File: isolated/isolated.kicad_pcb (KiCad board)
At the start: 2 copper layers, 110 x 33.8 mm, 59 parts, among them J1 Screw_Terminal_01x02, J2 Screw_Terminal_01x02, Q1 IRF3205, Q2 IRF3205, U1 LTC3723, U2 TCMT1103, U3 LT1431, U4 MCP1792x-5002xCB

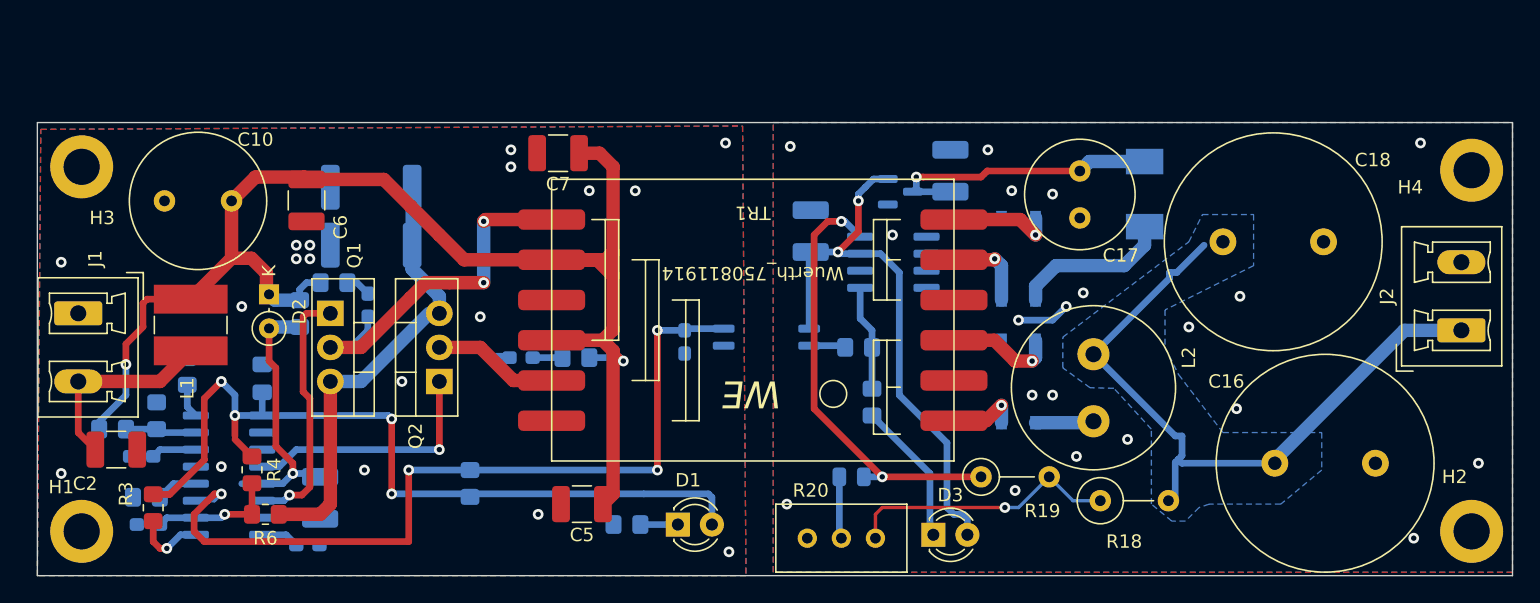
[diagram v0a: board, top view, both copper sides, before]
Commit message: kicad: Minor cleanups
- Replace LT1431 with TL431.

Signed-off-by: Patrick Rudolph <rudolphpatrick05@gmail.com>
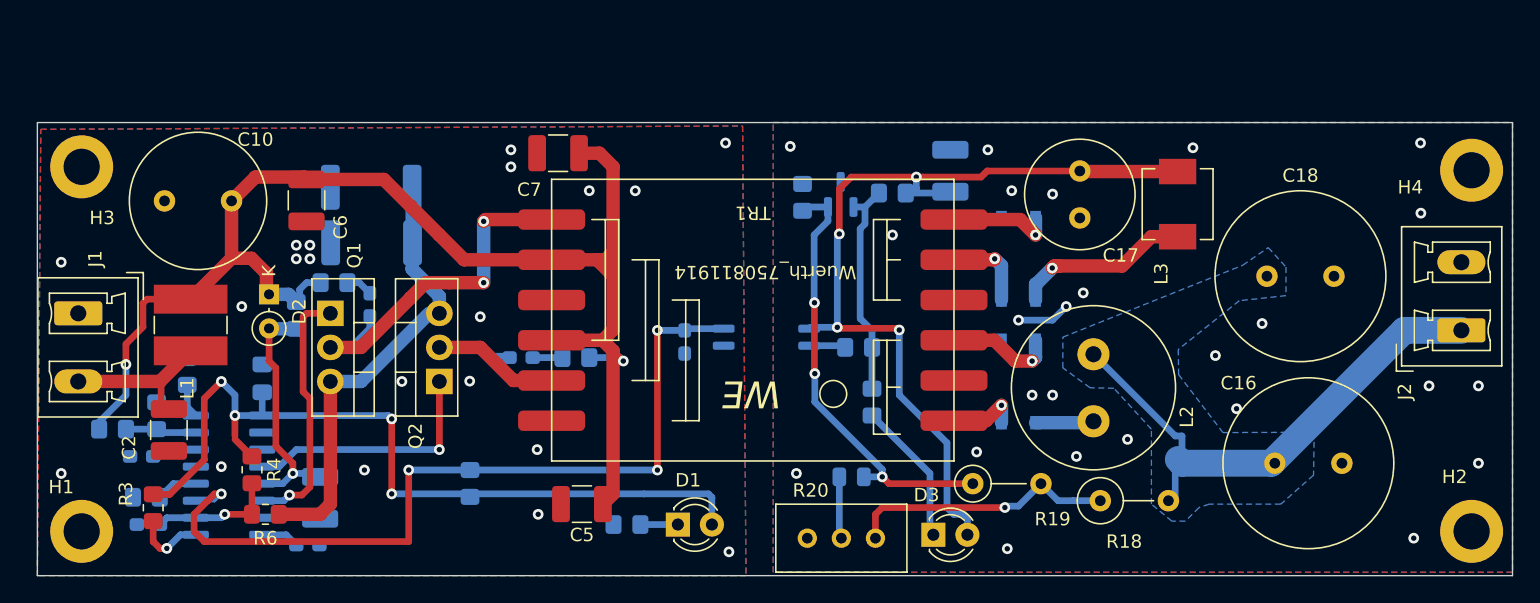
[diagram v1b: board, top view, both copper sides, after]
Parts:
- removed C19: 2u2, Capacitor_SMD:C_1210_3225Metric_Pad1.33x2.70mm_HandSolder
- removed U4: MCP1792x-5002xCB, Package_TO_SOT_SMD:SOT-23
- added R21: 10k, Resistor_SMD:R_0805_2012Metric_Pad1.20x1.40mm_HandSolder, B.Cu at (168.1, 40.3)
- added R22: 7k6, Resistor_SMD:R_0805_2012Metric_Pad1.20x1.40mm_HandSolder, B.Cu at (161.4, 40.6)
- C10: value C_Polarized -> 100u
- C16, C18: footprint Capacitor_THT:C_Radial_D16.0mm_H25.0mm_P7.50mm -> Capacitor_THT:C_Radial_D12.5mm_H20.0mm_P5.00mm
- C17: value 100u -> 10u
- L3: moved to F.Cu
- Q1, Q2: value IRF3205 -> IRLIZ 34N
- R15: value 330 -> 1k2
- R16: value 1k -> 3k3
- U3: value LT1431 -> TL431DBZ; footprint Package_SO:SOIC-8_3.9x4.9mm_P1.27mm -> Package_TO_SOT_SMD:SOT-23
- moved U3 6.40 mm to (164.3, 40.4), turned to 90 degrees
- moved C2 4.19 mm to (114.2, 58.0), turned to -90 degrees
- moved C18 4.16 mm to (196.1, 46.5)
- moved L3 2.57 mm to (189.4, 41.1)
- moved R19 0.80 mm to (174.1, 62.0)
- moved R2 0.29 mm to (123.7, 49.4)
- moved R11 0.18 mm to (129.3, 44.0)
- moved C11 0.15 mm to (129.2, 48.6)
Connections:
- C18 pad 2: Net-(C16-Pad1) -> GNDPWR
- D3 pad 2: +5VA -> VDD
- U2 pad 1: +5VA -> VDD
- U3 pad 2: unconnected-(U3-Pad2) -> /RTOP
- U3 pad 3: +5VA -> GNDPWR
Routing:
- net VDD: track 22.5 -> 66.0 mm, vias 1 -> 4
- net +5VA: track 42.7 -> 0.00 mm, vias 2 -> 0
- net Net-(C16-Pad1): track 51.1 -> 39.2 mm
- net Net-(R15-Pad2): track 7.89 -> 16.4 mm
- net Net-(C2-Pad1): track 14.9 -> 11.4 mm
- net /VIN: track 106.5 -> 103.2 mm
- net +10V: track 20.1 -> 18.3 mm
- net Net-(D5-Pad1): track 11.8 -> 13.2 mm, vias 0 -> 1
- net Net-(R10-Pad2): track 3.18 -> 2.55 mm
- net /RTOP: track 33.2 -> 33.0 mm, vias 2 -> 3
- net GNDPWR: vias 20 -> 25
- net GND: vias 18 -> 20

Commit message: kicad: Fix issues found in v0.1
- Change SOIC to SSOP package
- Fix MB4S pinout

Signed-off-by: Patrick Rudolph <rudolphpatrick05@gmail.com>
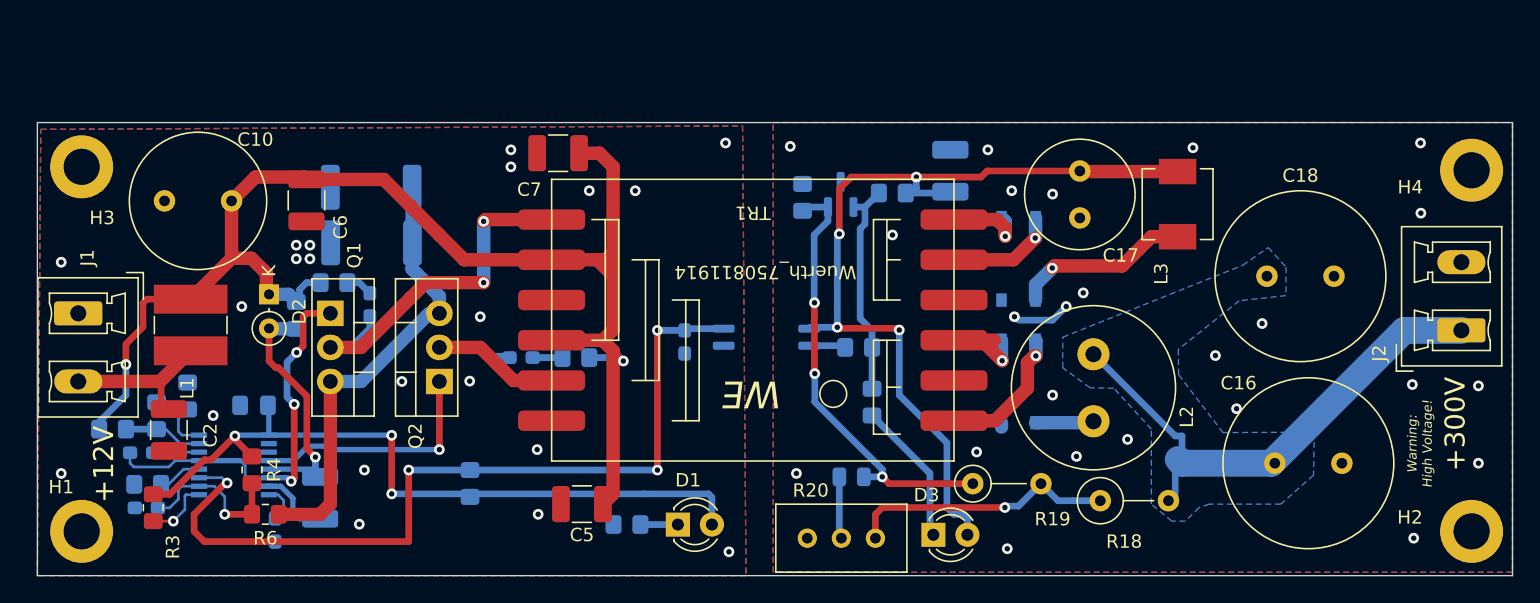
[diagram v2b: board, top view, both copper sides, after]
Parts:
- D5: value MB2S -> MB4S
- U1: footprint Package_SO:SOIC-16_3.9x9.9mm_P1.27mm -> Package_SO:SSOP-16_3.9x4.9mm_P0.635mm
- moved C4 2.68 mm to (122.1, 65.4), turned to -90 degrees
- moved C3 2.10 mm to (120.5, 56.1), turned to 0 degrees
- moved R10 1.83 mm to (115.6, 55.4)
- moved C8 1.25 mm to (112.5, 63.8)
- moved R7 0.97 mm to (112.6, 62.0)
- moved U1 0.85 mm to (119.0, 60.6)
- moved C12 0.28 mm to (112.2, 59.7)
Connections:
- D4 pad 2: Net-(D4-Pad2) -> GNDPWR
- D4 pad 3: GNDPWR -> Net-(TR1-Pad3)
- D4 pad 4: Net-(D4-Pad4) -> Net-(TR1-Pad1)
- D5 pad 2: Net-(D5-Pad2) -> GNDPWR
- D5 pad 3: GNDPWR -> Net-(TR1-Pad6)
- D5 pad 4: Net-(D5-Pad4) -> Net-(TR1-Pad5)
- TR1 pad 1: Net-(D4-Pad2) -> Net-(TR1-Pad1)
- TR1 pad 3: Net-(D4-Pad4) -> Net-(TR1-Pad3)
- TR1 pad 5: Net-(D5-Pad2) -> Net-(TR1-Pad5)
- TR1 pad 6: Net-(D5-Pad4) -> Net-(TR1-Pad6)
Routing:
- net GND: track 0.00 -> 18.3 mm, vias 20 -> 21
- net Net-(TR1-Pad1): track 0.00 -> 10.4 mm, vias 0 -> 1
- net +5V: track 62.9 -> 53.9 mm, vias 4 -> 3
- net Net-(TR1-Pad3): track 0.00 -> 8.78 mm, vias 0 -> 1
- net Net-(TR1-Pad5): track 0.00 -> 8.26 mm, vias 0 -> 1
- net Net-(D4-Pad4): track 8.13 -> 0.00 mm, vias 1 -> 0
- net Net-(D5-Pad4): track 7.86 -> 0.00 mm, vias 1 -> 0
- net Net-(D5-Pad2): track 6.35 -> 0.00 mm, vias 1 -> 0
- net Net-(TR1-Pad6): track 0.00 -> 6.23 mm, vias 0 -> 1
- net Net-(D4-Pad2): track 5.32 -> 0.00 mm, vias 1 -> 0
- net /CS: track 9.49 -> 12.1 mm
- net /DRVA: track 19.0 -> 17.0 mm, vias 1 -> 3
- net Net-(R10-Pad2): track 2.55 -> 3.59 mm
- net Net-(R12-Pad1): track 5.32 -> 6.26 mm
- net /COMP: track 61.6 -> 62.6 mm
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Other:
- board text added: "+12V"
- board text added: "+300V"
- board text added: "Warning: High Voltage!"

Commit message: doc/kicad: Update to revision v0.2
Fix the problems found in revision v0.1.

Revision v0.2 works much better and is able to power a
4W 240VAC LED bulb using 270VDC.

There are a couple of things to improve though.

Signed-off-by: Patrick Rudolph <rudolphpatrick05@gmail.com>
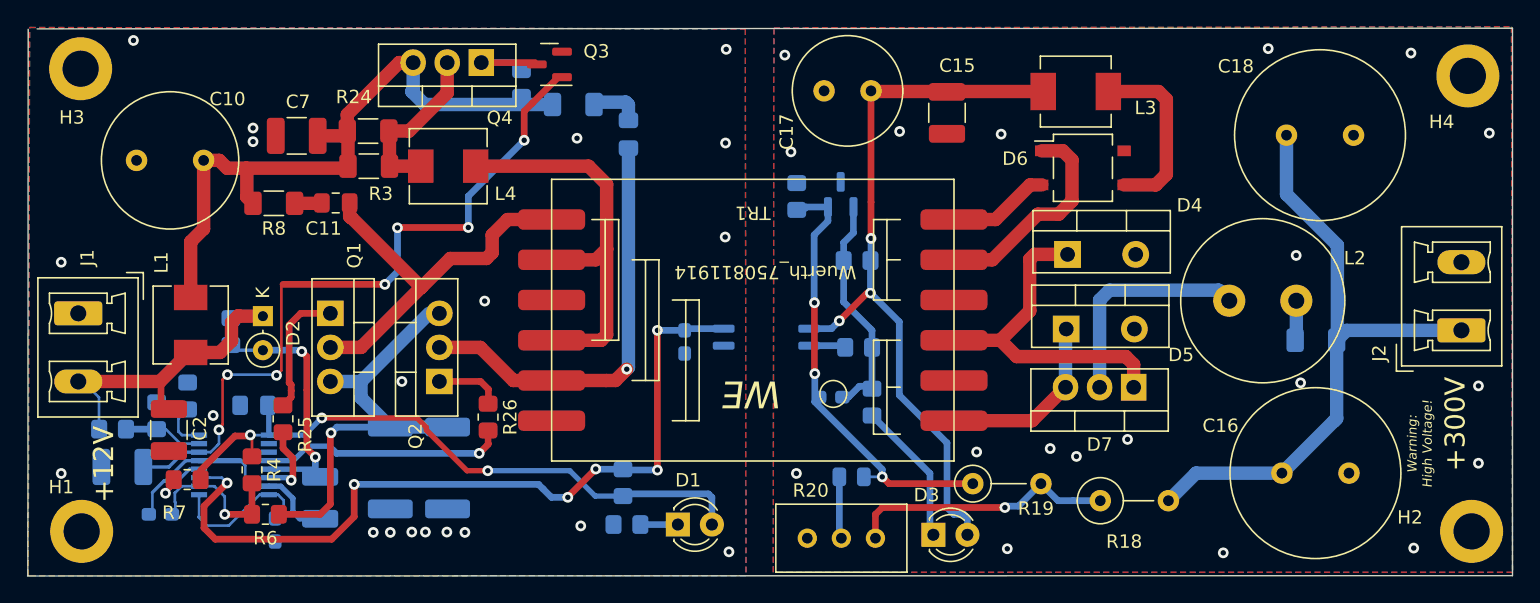
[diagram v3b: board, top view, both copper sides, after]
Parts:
- removed C6: 1u, Capacitor_SMD:C_1210_3225Metric_Pad1.33x2.70mm_HandSolder
- added D6: MB4S, Package_TO_SOT_SMD:TO-269AA, F.Cu at (182.3, 38.4)
- added D7: VS-HFA08TA60C-M3, Package_TO_SOT_THT:TO-220-3_Vertical, F.Cu at (186.1, 54.8)
- added L4: IHLP2020CZER4R7M1A, Inductor_SMD:L_Sunlord_MWSA05xxS, F.Cu at (135.0, 38.3)
- added Q3: 2N7002H, Package_TO_SOT_SMD:SOT-23, F.Cu at (142.6, 30.7)
- added Q4: FQP27P06, Package_TO_SOT_THT:TO-220-3_Vertical, F.Cu at (137.5, 30.6)
- added R23: 10k, Resistor_SMD:R_0805_2012Metric_Pad1.20x1.40mm_HandSolder, B.Cu at (140.5, 32.1)
- added R24: 1, Resistor_SMD:R_1206_3216Metric_Pad1.30x1.75mm_HandSolder, F.Cu at (129.0, 35.7)
- added R25: 0, Resistor_SMD:R_0805_2012Metric_Pad1.20x1.40mm_HandSolder, F.Cu at (122.7, 57.1)
- added R26: 0, Resistor_SMD:R_0805_2012Metric_Pad1.20x1.40mm_HandSolder, F.Cu at (138.0, 57.0)
- added R27: 0, Resistor_SMD:R_1206_3216Metric_Pad1.30x1.75mm_HandSolder, B.Cu at (199.7, 51.3)
- C11: value 100p -> 1n; footprint Capacitor_SMD:C_0603_1608Metric_Pad1.08x0.95mm_HandSolder -> Capacitor_SMD:C_0805_2012Metric_Pad1.18x1.45mm_HandSolder; moved to F.Cu
- C12: value 68n -> 1u; footprint Capacitor_SMD:C_0603_1608Metric_Pad1.08x0.95mm_HandSolder -> Capacitor_SMD:C_1210_3225Metric_Pad1.33x2.70mm_HandSolder
- C13: value 100p -> 1n; footprint Capacitor_SMD:C_0603_1608Metric_Pad1.08x0.95mm_HandSolder -> Capacitor_SMD:C_0805_2012Metric_Pad1.18x1.45mm_HandSolder
- C15: moved to F.Cu
- C16, C18: value 47u -> 4u7
- C4: value 560p -> 270p
- C5: value 1u -> 330p; footprint Capacitor_SMD:C_1210_3225Metric_Pad1.33x2.70mm_HandSolder -> Capacitor_SMD:C_0603_1608Metric_Pad1.08x0.95mm_HandSolder; moved to B.Cu
- C7: value 1u -> 10u
- D4, D5: value MB4S -> MBR735; footprint Package_TO_SOT_SMD:TO-269AA -> Package_TO_SOT_THT:TO-220-2_Vertical; moved to F.Cu
- L1: value L-242408FPS 3,3µ -> IHLP2020CZER4R7M1A; footprint Inductor_SMD:L_Ferrocore_DLG-0504 -> Inductor_SMD:L_Sunlord_MWSA05xxS
- L2: value L-11P 3,3M -> 7687480472
- R14: footprint Resistor_SMD:R_0805_2012Metric_Pad1.20x1.40mm_HandSolder -> Resistor_SMD:R_1206_3216Metric_Pad1.30x1.75mm_HandSolder
- R18, R19: value 270k -> 1meg
- R22: value 7k6 -> 12k
- R3: value 150k -> 1; footprint Resistor_SMD:R_0805_2012Metric_Pad1.20x1.40mm_HandSolder -> Resistor_SMD:R_1206_3216Metric_Pad1.30x1.75mm_HandSolder
- R7: value 33k -> 100k; moved to F.Cu
- R8: footprint Resistor_SMD:R_0805_2012Metric_Pad1.20x1.40mm_HandSolder -> Resistor_SMD:R_1206_3216Metric_Pad1.30x1.75mm_HandSolder; moved to F.Cu
- U1: value LTC3723 -> LTC3723-2
- moved R3 30.1 mm to (129.1, 38.3), turned to 0 degrees
- moved R9 21.0 mm to (130.7, 60.8), turned to -90 degrees
- moved C5 20.2 mm to (163.6, 55.5)
- moved C7 19.5 mm to (123.7, 36.0)
- moved R14 18.9 mm to (144.3, 33.7), turned to 0 degrees
- moved C13 18.5 mm to (148.5, 35.9), turned to -90 degrees
- moved R11 17.7 mm to (135.0, 60.8), turned to -90 degrees
- moved C17 16.7 mm to (166.5, 32.7), turned to 180 degrees
- moved L2 13.5 mm to (193.3, 48.3), turned to 0 degrees
- moved R5 11.4 mm to (148.1, 61.9)
- moved L3 11.3 mm to (181.8, 32.7), turned to 180 degrees
- moved C18 10.6 mm to (197.5, 36.0)
- moved D4 10.2 mm to (181.2, 44.9), turned to 0 degrees
- moved C11 8.01 mm to (126.6, 41.0), turned to 0 degrees
- moved R8 7.43 mm to (122.0, 41.1)
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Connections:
- C10 pad 1: /VIN -> Net-(Q4-Pad3)
- C2 pad 1: Net-(C2-Pad1) -> /VIN
- C5 pad 1: /VIN -> Net-(C5-Pad1)
- C5 pad 2: GND -> /RTOP
- C7 pad 1: /VIN -> Net-(Q4-Pad3)
- D4 pad 1: Net-(L2-Pad1) -> Net-(D4-Pad1)
- D5 pad 1: Net-(L3-Pad1) -> Net-(D5-Pad1)
- J1 pad 2: Net-(C2-Pad1) -> /VIN
- L1 pad 1: Net-(C2-Pad1) -> /VIN
- L1 pad 2: /VIN -> Net-(Q4-Pad3)
- L2 pad 1: Net-(L2-Pad1) -> Net-(D7-Pad2)
- L2 pad 2: Net-(C16-Pad1) -> Net-(L2-Pad2)
- Q1 pad 1: /DRVA -> Net-(Q1-Pad1)
- Q2 pad 1: /DRVB -> Net-(Q2-Pad1)
- R14 pad 1: /VIN -> Net-(Q4-Pad3)
- R15 pad 2: Net-(R15-Pad2) -> Net-(C5-Pad1)
- R16 pad 1: Net-(R15-Pad2) -> Net-(C5-Pad1)
- R21 pad 1: Net-(R15-Pad2) -> Net-(C5-Pad1)
- R3 pad 1: +5V -> Net-(Q4-Pad3)
- R3 pad 2: Net-(R3-Pad2) -> Net-(L4-Pad1)
- R7 pad 1: GND -> +5V
- R8 pad 1: /VIN -> Net-(Q4-Pad3)
- TR1 pad 1: Net-(TR1-Pad1) -> Net-(D5-Pad1)
- TR1 pad 10: /VIN -> Net-(L4-Pad2)
- TR1 pad 3: Net-(TR1-Pad3) -> Net-(D4-Pad1)
- TR1 pad 8: /VIN -> Net-(L4-Pad2)
- U1 pad 9: Net-(R3-Pad2) -> Net-(C4-Pad1)
- U3 pad 1: Net-(R15-Pad2) -> Net-(C5-Pad1)
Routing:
- net /VIN: track 103.2 -> 25.6 mm, vias 2 -> 0
- net Net-(C12-Pad1): track 3.44 -> 54.2 mm, vias 0 -> 7
- net Net-(Q4-Pad3): track 0.00 -> 50.4 mm
- net Net-(L4-Pad2): track 0.00 -> 30.4 mm
- net Net-(D4-Pad1): track 0.00 -> 25.8 mm
- net Net-(C13-Pad2): track 14.5 -> 31.9 mm, vias 0 -> 1
- net Net-(C5-Pad1): track 0.00 -> 17.3 mm
- net Net-(D7-Pad2): track 0.00 -> 16.8 mm
- net Net-(R15-Pad2): track 16.4 -> 0.00 mm
- net Net-(D5-Pad1): track 0.00 -> 13.7 mm
- net Net-(L4-Pad1): track 0.00 -> 12.8 mm
- net Net-(C2-Pad1): track 11.4 -> 0.00 mm
- net /DRVA: track 17.0 -> 5.69 mm, vias 3 -> 1
- net VDD: track 66.2 -> 55.6 mm, vias 4 -> 3
- net Net-(TR1-Pad1): track 10.4 -> 0.00 mm, vias 1 -> 0
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- removed copper zone on B.Cu, net Net-(C16-Pad1)
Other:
- board size 110 x 33.8 mm -> 110.7 x 40.8 mm
